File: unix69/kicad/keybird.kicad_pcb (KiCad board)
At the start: 2 copper layers, 142 parts, among them SW00 SW_Push, SW01 SW_Push, SW02 SW_Push, SW03 SW_Push, SW04 SW_Push, SW05 SW_Push, SW06 SW_Push, SW07 SW_Push, SW10 SW_Push, SW11 SW_Push, SW12 SW_Push, SW13 SW_Push, SW14 SW_Push, SW15 SW_Push, SW16 SW_Push, SW17 SW_Push, SW20 SW_Push, SW21 SW_Push, SW22 SW_Push, SW23 SW_Push, SW24 SW_Push, SW25 SW_Push, SW26 SW_Push, SW27 SW_Push, SW30 SW_Push, SW31 SW_Push, SW32 SW_Push, SW33 SW_Push, SW34 SW_Push, SW35 SW_Push, SW36 SW_Push, SW40 SW_Push, SW41 SW_Push, SW42 SW_Push, SW43 SW_Push, SW44 SW_Push, SW45 SW_Push, SW47 SW_Push, SW50 SW_Push, SW51 SW_Push, SW52 SW_Push, SW53 SW_Push, SW54 SW_Push, SW55 SW_Push, SW56 SW_Push, SW57 SW_Push, SW60 SW_Push, SW61 SW_Push, SW62 SW_Push, SW63 SW_Push, SW64 SW_Push, SW65 SW_Push, SW66 SW_Push, SW67 SW_Push, SW70 SW_Push, SW71 SW_Push, SW72 SW_Push, SW73 SW_Push, SW74 SW_Push, SW75 SW_Push, SW76 SW_Push, SW77 SW_Push, SW80 SW_Push, SW81 SW_Push, SW83 SW_Push, SW84 SW_Push, SW85 SW_Push, SW86 SW_Push, SW87 SW_Push, U0 RP2040-Tiny

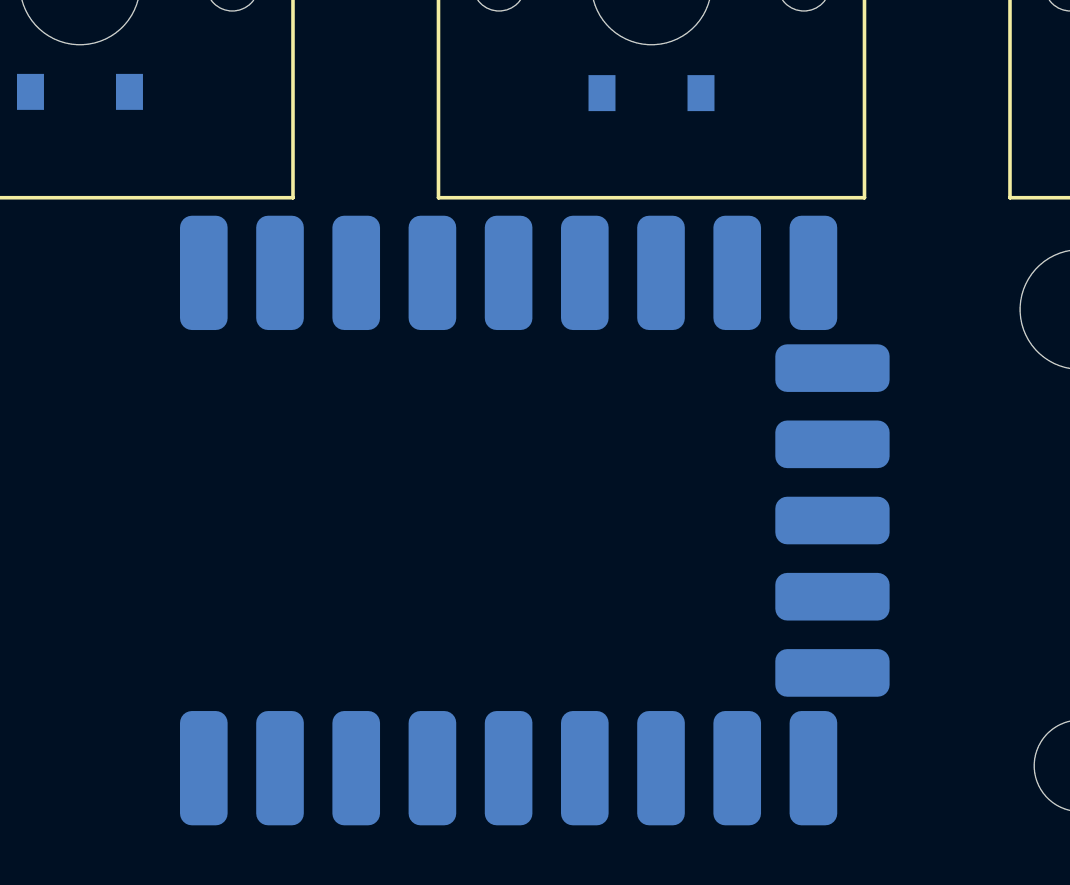
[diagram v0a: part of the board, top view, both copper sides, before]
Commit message: much pcb fettling
silkscreen key names from schematic

diode placement wrt switch connections
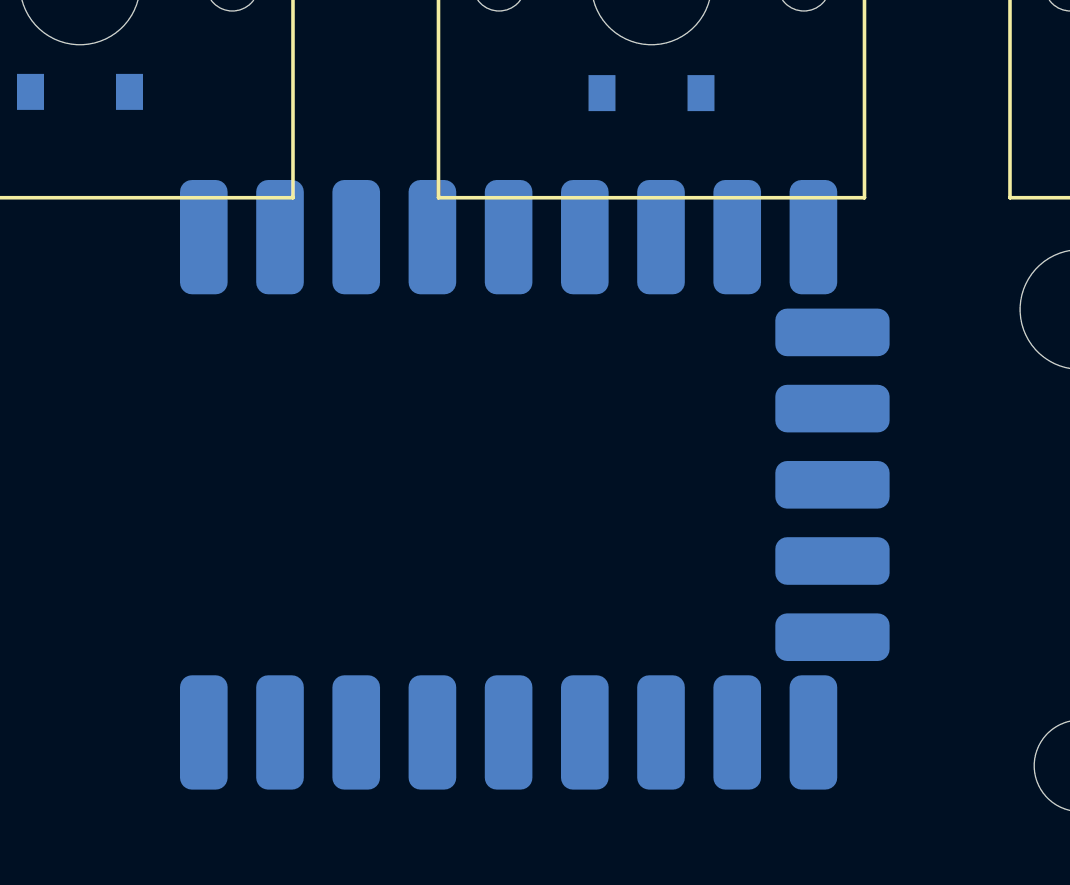
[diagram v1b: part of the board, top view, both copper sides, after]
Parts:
- SW00: value SW_Push -> ESC
- SW01: value SW_Push -> 2
- SW02: value SW_Push -> 4
- SW03: value SW_Push -> 6
- SW04: value SW_Push -> 8
- SW05: value SW_Push -> 0
- SW06: value SW_Push -> EQUAL
- SW07: value SW_Push -> GRAVE
- SW10: value SW_Push -> 1
- SW11: value SW_Push -> 3
- SW12: value SW_Push -> 5
- SW13: value SW_Push -> 7
- SW14: value SW_Push -> 9
- SW15: value SW_Push -> MINUS
- SW16: value SW_Push -> BSLS
- SW17: value SW_Push -> F16
- SW20: value SW_Push -> TAB
- SW21: value SW_Push -> W
- SW22: value SW_Push -> R
- SW23: value SW_Push -> Y
- SW24: value SW_Push -> I
- SW25: value SW_Push -> P
- SW26: value SW_Push -> RBRC
- SW27: value SW_Push -> F17
- SW30: value SW_Push -> Q
- SW31: value SW_Push -> E
- SW32: value SW_Push -> T
- SW33: value SW_Push -> U
- SW34: value SW_Push -> O
- SW35: value SW_Push -> LBRC
- SW36: value SW_Push -> BSPC
- SW40: value SW_Push -> A
- SW41: value SW_Push -> D
- SW42: value SW_Push -> G
- SW43: value SW_Push -> J
- SW44: value SW_Push -> L
- SW45: value SW_Push -> QUOTE
- SW47: value SW_Push -> F18
- SW50: value SW_Push -> LCTL
- SW51: value SW_Push -> S
- SW52: value SW_Push -> F
- SW53: value SW_Push -> H
- SW54: value SW_Push -> K
- SW55: value SW_Push -> SCLN
- SW56: value SW_Push -> ENTER
- SW57: value SW_Push -> F19
- SW60: value SW_Push -> LSFT
- SW61: value SW_Push -> X
- SW62: value SW_Push -> V
- SW63: value SW_Push -> N
- SW64: value SW_Push -> COMMA
- SW65: value SW_Push -> SLASH
- SW66: value SW_Push -> RSFT
- SW67: value SW_Push -> UP
- SW70: value SW_Push -> LFN
- SW71: value SW_Push -> Z
- SW72: value SW_Push -> C
- SW73: value SW_Push -> B
- SW74: value SW_Push -> M
- SW75: value SW_Push -> DOT
- SW76: value SW_Push -> LEFT
- SW77: value SW_Push -> RIGHT
- SW80: value SW_Push -> LALT
- SW81: value SW_Push -> LGUI
- SW83: value SW_Push -> SPACE
- SW84: value SW_Push -> RGUI
- SW85: value SW_Push -> RCTL
- SW86: value SW_Push -> RFN
- SW87: value SW_Push -> DOWN
- moved U0 1.19 mm to (176.2, 97.6)

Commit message: pcb edge and cutout for reset buttons
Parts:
- moved D04 8.06 mm to (179.8, 20.2), turned to 180 degrees
- moved D13 8.06 mm to (153.6, 20.2), turned to 180 degrees
- turned SW04 to 180 degrees
- turned SW13 to 180 degrees
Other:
- board outline added: 304.8 x 95.2 mm

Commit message: connecting tracks to diodes
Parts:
- moved D04 1.33 mm to (178.5, 20.2)
- moved D13 1.19 mm to (154.8, 20.2)
- moved D40 0.30 mm to (57.1, 65.5)
- moved D47 0.25 mm to (309.6, 65.5)
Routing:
- net /GP7: track 0.00 -> 10.7 mm
- net Net-(D04-Pad1): track 0.00 -> 10.7 mm
- net Net-(D17-Pad1): track 0.00 -> 9.90 mm
- net Net-(D64-Pad1): track 0.00 -> 9.68 mm
- net Net-(D87-Pad1): track 0.00 -> 9.68 mm
- net Net-(D67-Pad1): track 0.00 -> 9.68 mm
- net Net-(D75-Pad1): track 0.00 -> 9.68 mm
- net Net-(D65-Pad1): track 0.00 -> 9.68 mm
- net Net-(D07-Pad1): track 0.00 -> 9.68 mm
- net Net-(D86-Pad1): track 0.00 -> 9.68 mm
- net Net-(D06-Pad1): track 0.00 -> 9.68 mm
- net Net-(D74-Pad1): track 0.00 -> 9.68 mm
- net Net-(D73-Pad1): track 0.00 -> 9.68 mm
- net Net-(D63-Pad1): track 0.00 -> 9.68 mm
- net Net-(D62-Pad1): track 0.00 -> 9.68 mm
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
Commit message: redo the row lines on the front of the board
much nicer!
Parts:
- moved U2040 61.9 mm to (114.3, 98.2)
- moved D04 1.44 mm to (179.8, 19.6), turned to 0 degrees
- moved D13 1.14 mm to (153.8, 19.6), turned to 0 degrees
- moved D16 0.60 mm to (271.4, 28.0)
- moved D17 0.60 mm to (309.6, 28.0)
- moved D07 0.60 mm to (290.5, 28.0)
- moved D15 0.60 mm to (233.4, 28.0)
- moved D63 0.60 mm to (161.9, 85.1)
- moved D66 0.60 mm to (264.3, 85.1)
- moved D47 0.60 mm to (309.6, 66.1)
- moved D40 0.57 mm to (57.1, 66.1)
- moved D06 0.56 mm to (252.4, 28.0)
- moved D70 0.55 mm to (26.2, 104.2)
- moved D76 0.55 mm to (271.5, 104.2)
- moved D80 0.55 mm to (50.0, 104.2)
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- renumbered U0 to U2040
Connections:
- net /GP10 renamed /COL5
- net /GP11 renamed /COL6
- net /GP12 renamed /COL7
- net /GP13 renamed /COL3
- net /GP14 renamed /COL2
- net /GP15 renamed /COL1
- net /GP26 renamed /COL0
- net /GP4 renamed /ROW4
- net /GP9 renamed /COL4
- D00 pad 2: /GP8 -> /ROW0
- D01 pad 2: /GP8 -> /ROW0
- D02 pad 2: /GP8 -> /ROW0
- D03 pad 2: /GP8 -> /ROW0
- D04 pad 2: /GP8 -> /ROW0
- D05 pad 2: /GP8 -> /ROW0
- D06 pad 2: /GP8 -> /ROW0
- D07 pad 2: /GP8 -> /ROW0
- D10 pad 2: /GP7 -> /ROW1
- D11 pad 2: /GP7 -> /ROW1
- D12 pad 2: /GP7 -> /ROW1
- D13 pad 2: /GP7 -> /ROW1
- D14 pad 2: /GP7 -> /ROW1
- D15 pad 2: /GP7 -> /ROW1
- D16 pad 2: /GP7 -> /ROW1
- D17 pad 2: /GP7 -> /ROW1
- D20 pad 2: /GP6 -> /ROW2
- D21 pad 2: /GP6 -> /ROW2
- D22 pad 2: /GP6 -> /ROW2
- D23 pad 2: /GP6 -> /ROW2
- D24 pad 2: /GP6 -> /ROW2
- D25 pad 2: /GP6 -> /ROW2
- D26 pad 2: /GP6 -> /ROW2
- D27 pad 2: /GP6 -> /ROW2
- D30 pad 2: /GP5 -> /ROW3
- D31 pad 2: /GP5 -> /ROW3
- D32 pad 2: /GP5 -> /ROW3
- D33 pad 2: /GP5 -> /ROW3
- D34 pad 2: /GP5 -> /ROW3
- D35 pad 2: /GP5 -> /ROW3
- D36 pad 2: /GP5 -> /ROW3
- D50 pad 2: /GP3 -> /ROW5
- D51 pad 2: /GP3 -> /ROW5
- D52 pad 2: /GP3 -> /ROW5
- D53 pad 2: /GP3 -> /ROW5
- D54 pad 2: /GP3 -> /ROW5
- D55 pad 2: /GP3 -> /ROW5
- D56 pad 2: /GP3 -> /ROW5
- D57 pad 2: /GP3 -> /ROW5
- D60 pad 2: /GP2 -> /ROW6
- D61 pad 2: /GP2 -> /ROW6
- D62 pad 2: /GP2 -> /ROW6
- D63 pad 2: /GP2 -> /ROW6
- D64 pad 2: /GP2 -> /ROW6
- D65 pad 2: /GP2 -> /ROW6
- D66 pad 2: /GP2 -> /ROW6
- D67 pad 2: /GP2 -> /ROW6
- D70 pad 2: /GP1 -> /ROW7
- D71 pad 2: /GP1 -> /ROW7
- D72 pad 2: /GP1 -> /ROW7
- D73 pad 2: /GP1 -> /ROW7
- D74 pad 2: /GP1 -> /ROW7
- D75 pad 2: /GP1 -> /ROW7
- D76 pad 2: /GP1 -> /ROW7
- D77 pad 2: /GP1 -> /ROW7
- D80 pad 2: /GP0 -> /ROW8
- D81 pad 2: /GP0 -> /ROW8
- D83 pad 2: /GP0 -> /ROW8
- D84 pad 2: /GP0 -> /ROW8
- D85 pad 2: /GP0 -> /ROW8
- D86 pad 2: /GP0 -> /ROW8
- D87 pad 2: /GP0 -> /ROW8
- U2040 pad 0: /GP0 -> /ROW0
- U2040 pad 1: /GP1 -> /ROW1
- U2040 pad 2: /GP2 -> /ROW2
- U2040 pad 3: /GP3 -> /ROW3
- U2040 pad 5: /GP5 -> /ROW5
- U2040 pad 6: /GP6 -> /ROW6
- U2040 pad 7: /GP7 -> /ROW7
- U2040 pad 8: /GP8 -> /ROW8
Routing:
- net /ROW1: track 0.00 -> 514.9 mm, vias 0 -> 9
- net /ROW7: track 0.00 -> 507.3 mm, vias 0 -> 9
- net /ROW0: track 0.00 -> 493.8 mm, vias 0 -> 9
- net /ROW5: track 0.00 -> 488.4 mm, vias 0 -> 9
- net /ROW2: track 0.00 -> 476.6 mm, vias 0 -> 9
- net /ROW3: track 0.00 -> 447.8 mm, vias 0 -> 8
- net /ROW4: track 7.14 -> 453.4 mm, vias 0 -> 8
- net /ROW6: track 0.00 -> 421.3 mm, vias 0 -> 9
- net /ROW8: track 0.00 -> 267.0 mm, vias 0 -> 8
- net (no net): track 0.00 -> 186.3 mm, vias 69 -> 0
- net /GP7: track 10.7 -> 0.00 mm
- net /GP6: track 9.53 -> 0.00 mm
- net /GP3: track 9.53 -> 0.00 mm
- net /GP1: track 9.53 -> 0.00 mm
- net /GP2: track 9.53 -> 0.00 mm
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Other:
- board text added: "RP2040 is under here"
- board text added: "Tony Finch <dot@dotat.at>"
- board text added: "desiged and assembled"
- board text added: "in Cambridge by"
- board text added: "my usb port is too big"

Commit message: done? no drc errors!
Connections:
- U2040 pad 10: /COL5 -> /COL6
- U2040 pad 11: /COL6 -> /COL5
- U2040 pad 12: /COL7 -> /COL4
- U2040 pad 14: /COL2 -> /COL0
- U2040 pad 16: /COL0 -> /COL2
- U2040 pad 9: /COL4 -> /COL7
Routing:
- net /COL7: track 0.00 -> 323.4 mm
- net /COL6: track 0.00 -> 321.3 mm
- net /COL5: track 0.00 -> 294.3 mm
- net /COL0: track 0.00 -> 286.6 mm
- net /COL4: track 0.00 -> 260.7 mm
- net /COL1: track 0.00 -> 245.8 mm
- net /COL2: track 0.00 -> 197.0 mm
- net /COL3: track 0.00 -> 174.8 mm
- net /ROW4: track 453.4 -> 455.1 mm
- net Net-(D14-Pad1): track 9.58 -> 10.2 mm
- net Net-(D80-Pad1): track 10.7 -> 10.1 mm

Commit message: final version with rows on front
gonna start again, this time better
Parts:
- renumbered U2040 to U1
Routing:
- net /COL1: track 245.8 -> 236.7 mm
- net /COL5: track 294.3 -> 287.5 mm
- net /COL4: track 260.7 -> 254.6 mm
- net /COL2: track 197.0 -> 191.8 mm
- net /COL0: track 286.6 -> 289.8 mm
- net /COL6: track 321.3 -> 318.5 mm
- net /COL3: track 174.8 -> 172.2 mm
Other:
- board text added: "(delete)"
- board text added: "(return)"
- board text added: "S P A C E"
- board text added: "rows on the other side"

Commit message: major revision
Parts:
- removed D75: DIODE, Diode_SMD:D_SOD-123
- removed SW75: DOT, Switch_Keyboard_Hotswap_Kailh:SW_Hotswap_Kailh_MX_1.00u
- added D82: DIODE, Diode_SMD:D_SOD-123, B.Cu at (83.9, 100.0)
- added SW82: LMETA, Switch_Keyboard_Hotswap_Kailh:SW_Hotswap_Kailh_MX_1.25u, F.Cu at (73.8, 100.1)
- SW07: value GRAVE -> BQUOT
- SW16: value BSLS -> BSLSH
- SW17: value F16 -> F13
- SW26: value RBRC -> RBRAC
- SW27: value F17 -> F14
- SW35: value LBRC -> LBRAC
- SW36: value BSPC -> DEL
- SW47: value F18 -> F15
- SW50: value LCTL -> LCTRL
- SW55: value SCLN -> COLON
- SW56: value ENTER -> RET
- SW57: value F19 -> F16
- SW60: value LSFT -> LSHFT
- SW66: value RSFT -> RSHFT
- SW70: value LFN -> Z; footprint Switch_Keyboard_Hotswap_Kailh:SW_Hotswap_Kailh_MX_1.25u -> Switch_Keyboard_Hotswap_Kailh:SW_Hotswap_Kailh_MX_1.00u
- SW71: value Z -> C
- SW72: value C -> B
- SW73: value B -> M
- SW74: value M -> DOT
- SW80: value LALT -> LFUN
- SW81: value LGUI -> LALT
- SW84: value RGUI -> RMETA
- SW85: value RCTL -> RCTRL
- SW86: value RFN -> RFUN
- moved SW70 44.7 mm to (66.7, 81.0)
- moved D70 39.3 mm to (59.5, 83.3), turned to 90 degrees
- moved SW74 38.1 mm to (219.1, 81.0)
- moved SW73 38.1 mm to (181.0, 81.0)
- moved SW72 38.1 mm to (142.9, 81.0)
- moved SW71 38.1 mm to (104.8, 81.0)
- moved D74 31.0 mm to (211.9, 83.3), turned to 90 degrees
- moved D73 31.0 mm to (173.8, 83.3), turned to 90 degrees
- moved D72 31.0 mm to (135.7, 83.3), turned to 90 degrees
- moved D71 31.0 mm to (97.6, 83.3), turned to 90 degrees
- moved SW80 23.8 mm to (26.2, 100.0), turned to 180 degrees
- moved SW81 23.8 mm to (50.0, 100.0), turned to 180 degrees
- moved D13 15.9 mm to (165.0, 30.9), turned to 90 degrees
- moved D80 14.3 mm to (36.3, 100.0), turned to -90 degrees
- moved D81 14.3 mm to (60.1, 100.0), turned to -90 degrees
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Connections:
- D70 pad 1: Net-(D70-Pad1) -> Net-(SW70-Pad1)
- D71 pad 1: Net-(D71-Pad1) -> Net-(SW71-Pad1)
- D72 pad 1: Net-(D72-Pad1) -> Net-(SW72-Pad1)
- D73 pad 1: Net-(D73-Pad1) -> Net-(SW73-Pad1)
- D74 pad 1: Net-(D74-Pad1) -> Net-(SW74-Pad1)
- D76 pad 1: Net-(D76-Pad1) -> Net-(SW76-Pad1)
- SW00 pad 1: /COL0 -> Net-(D00-Pad1)
- SW00 pad 2: Net-(D00-Pad1) -> /COL0
- SW01 pad 1: /COL1 -> Net-(D01-Pad1)
- SW01 pad 2: Net-(D01-Pad1) -> /COL1
- SW02 pad 1: /COL2 -> Net-(D02-Pad1)
- SW02 pad 2: Net-(D02-Pad1) -> /COL2
- SW03 pad 1: /COL3 -> Net-(D03-Pad1)
- SW03 pad 2: Net-(D03-Pad1) -> /COL3
- SW04 pad 1: /COL4 -> Net-(D04-Pad1)
- SW04 pad 2: Net-(D04-Pad1) -> /COL4
- SW05 pad 1: /COL5 -> Net-(D05-Pad1)
- SW05 pad 2: Net-(D05-Pad1) -> /COL5
- SW06 pad 1: /COL6 -> Net-(D06-Pad1)
- SW06 pad 2: Net-(D06-Pad1) -> /COL6
- SW07 pad 1: /COL7 -> Net-(D07-Pad1)
- SW07 pad 2: Net-(D07-Pad1) -> /COL7
- SW10 pad 1: /COL0 -> Net-(D10-Pad1)
- SW10 pad 2: Net-(D10-Pad1) -> /COL0
- SW11 pad 1: /COL1 -> Net-(D11-Pad1)
- SW11 pad 2: Net-(D11-Pad1) -> /COL1
- SW12 pad 1: /COL2 -> Net-(D12-Pad1)
- SW12 pad 2: Net-(D12-Pad1) -> /COL2
- SW13 pad 1: /COL3 -> Net-(D13-Pad1)
- SW13 pad 2: Net-(D13-Pad1) -> /COL3
- SW14 pad 1: /COL4 -> Net-(D14-Pad1)
- SW14 pad 2: Net-(D14-Pad1) -> /COL4
- SW15 pad 1: /COL5 -> Net-(D15-Pad1)
- SW15 pad 2: Net-(D15-Pad1) -> /COL5
- SW16 pad 1: /COL6 -> Net-(D16-Pad1)
- SW16 pad 2: Net-(D16-Pad1) -> /COL6
- SW17 pad 1: /COL7 -> Net-(D17-Pad1)
- SW17 pad 2: Net-(D17-Pad1) -> /COL7
- SW20 pad 1: /COL0 -> Net-(D20-Pad1)
- SW20 pad 2: Net-(D20-Pad1) -> /COL0
- SW21 pad 1: /COL1 -> Net-(D21-Pad1)
- SW21 pad 2: Net-(D21-Pad1) -> /COL1
- SW22 pad 1: /COL2 -> Net-(D22-Pad1)
- SW22 pad 2: Net-(D22-Pad1) -> /COL2
- SW23 pad 1: /COL3 -> Net-(D23-Pad1)
- SW23 pad 2: Net-(D23-Pad1) -> /COL3
- SW24 pad 1: /COL4 -> Net-(D24-Pad1)
- SW24 pad 2: Net-(D24-Pad1) -> /COL4
- SW25 pad 1: /COL5 -> Net-(D25-Pad1)
- SW25 pad 2: Net-(D25-Pad1) -> /COL5
- SW26 pad 1: /COL6 -> Net-(D26-Pad1)
- SW26 pad 2: Net-(D26-Pad1) -> /COL6
- SW27 pad 1: /COL7 -> Net-(D27-Pad1)
- SW27 pad 2: Net-(D27-Pad1) -> /COL7
- SW30 pad 1: /COL0 -> Net-(D30-Pad1)
- SW30 pad 2: Net-(D30-Pad1) -> /COL0
- SW31 pad 1: /COL1 -> Net-(D31-Pad1)
- SW31 pad 2: Net-(D31-Pad1) -> /COL1
- SW32 pad 1: /COL2 -> Net-(D32-Pad1)
- SW32 pad 2: Net-(D32-Pad1) -> /COL2
- SW33 pad 1: /COL3 -> Net-(D33-Pad1)
- SW33 pad 2: Net-(D33-Pad1) -> /COL3
- SW34 pad 1: /COL4 -> Net-(D34-Pad1)
- SW34 pad 2: Net-(D34-Pad1) -> /COL4
- SW35 pad 1: /COL5 -> Net-(D35-Pad1)
- SW35 pad 2: Net-(D35-Pad1) -> /COL5
- SW36 pad 1: /COL6 -> Net-(D36-Pad1)
- SW36 pad 2: Net-(D36-Pad1) -> /COL6
- SW40 pad 1: /COL0 -> Net-(D40-Pad1)
- SW40 pad 2: Net-(D40-Pad1) -> /COL0
- SW41 pad 1: /COL1 -> Net-(D41-Pad1)
- SW41 pad 2: Net-(D41-Pad1) -> /COL1
- SW42 pad 1: /COL2 -> Net-(D42-Pad1)
- SW42 pad 2: Net-(D42-Pad1) -> /COL2
- SW43 pad 1: /COL3 -> Net-(D43-Pad1)
- SW43 pad 2: Net-(D43-Pad1) -> /COL3
- SW44 pad 1: /COL4 -> Net-(D44-Pad1)
- SW44 pad 2: Net-(D44-Pad1) -> /COL4
- SW45 pad 1: /COL5 -> Net-(D45-Pad1)
- SW45 pad 2: Net-(D45-Pad1) -> /COL5
- SW47 pad 1: /COL7 -> Net-(D47-Pad1)
- SW47 pad 2: Net-(D47-Pad1) -> /COL7
- SW50 pad 1: /COL0 -> Net-(D50-Pad1)
- SW50 pad 2: Net-(D50-Pad1) -> /COL0
- SW51 pad 1: /COL1 -> Net-(D51-Pad1)
- SW51 pad 2: Net-(D51-Pad1) -> /COL1
- SW52 pad 1: /COL2 -> Net-(D52-Pad1)
- SW52 pad 2: Net-(D52-Pad1) -> /COL2
- SW53 pad 1: /COL3 -> Net-(D53-Pad1)
- SW53 pad 2: Net-(D53-Pad1) -> /COL3
- SW54 pad 1: /COL4 -> Net-(D54-Pad1)
- SW54 pad 2: Net-(D54-Pad1) -> /COL4
- SW55 pad 1: /COL5 -> Net-(D55-Pad1)
- SW55 pad 2: Net-(D55-Pad1) -> /COL5
- SW56 pad 1: /COL6 -> Net-(D56-Pad1)
- SW56 pad 2: Net-(D56-Pad1) -> /COL6
- SW57 pad 1: /COL7 -> Net-(D57-Pad1)
- SW57 pad 2: Net-(D57-Pad1) -> /COL7
- SW60 pad 1: /COL0 -> Net-(D60-Pad1)
- SW60 pad 2: Net-(D60-Pad1) -> /COL0
- SW61 pad 1: /COL1 -> Net-(D61-Pad1)
- SW61 pad 2: Net-(D61-Pad1) -> /COL1
- SW62 pad 1: /COL2 -> Net-(D62-Pad1)
- SW62 pad 2: Net-(D62-Pad1) -> /COL2
- SW63 pad 1: /COL3 -> Net-(D63-Pad1)
- SW63 pad 2: Net-(D63-Pad1) -> /COL3
- SW64 pad 1: /COL4 -> Net-(D64-Pad1)
- SW64 pad 2: Net-(D64-Pad1) -> /COL4
- SW65 pad 1: /COL5 -> Net-(D65-Pad1)
- SW65 pad 2: Net-(D65-Pad1) -> /COL5
- SW66 pad 1: /COL6 -> Net-(D66-Pad1)
- SW66 pad 2: Net-(D66-Pad1) -> /COL6
- SW67 pad 1: /COL7 -> Net-(D67-Pad1)
- SW67 pad 2: Net-(D67-Pad1) -> /COL7
- SW70 pad 1: /COL0 -> Net-(SW70-Pad1)
- SW70 pad 2: Net-(D70-Pad1) -> /COL0
- SW71 pad 1: /COL1 -> Net-(SW71-Pad1)
- SW71 pad 2: Net-(D71-Pad1) -> /COL1
- SW72 pad 1: /COL2 -> Net-(SW72-Pad1)
- SW72 pad 2: Net-(D72-Pad1) -> /COL2
- SW73 pad 1: /COL3 -> Net-(SW73-Pad1)
- SW73 pad 2: Net-(D73-Pad1) -> /COL3
- SW74 pad 1: /COL4 -> Net-(SW74-Pad1)
- SW74 pad 2: Net-(D74-Pad1) -> /COL4
- SW76 pad 1: /COL6 -> Net-(SW76-Pad1)
- SW76 pad 2: Net-(D76-Pad1) -> /COL6
- SW77 pad 1: /COL7 -> Net-(D77-Pad1)
- SW77 pad 2: Net-(D77-Pad1) -> /COL7
- SW80 pad 1: /COL0 -> Net-(D80-Pad1)
- SW80 pad 2: Net-(D80-Pad1) -> /COL0
- SW81 pad 1: /COL1 -> Net-(D81-Pad1)
- SW81 pad 2: Net-(D81-Pad1) -> /COL1
- SW83 pad 1: /COL3 -> Net-(D83-Pad1)
- SW83 pad 2: Net-(D83-Pad1) -> /COL3
- SW84 pad 1: /COL4 -> Net-(D84-Pad1)
- SW84 pad 2: Net-(D84-Pad1) -> /COL4
- SW85 pad 1: /COL5 -> Net-(D85-Pad1)
- SW85 pad 2: Net-(D85-Pad1) -> /COL5
- SW86 pad 1: /COL6 -> Net-(D86-Pad1)
- SW86 pad 2: Net-(D86-Pad1) -> /COL6
- SW87 pad 1: /COL7 -> Net-(D87-Pad1)
- SW87 pad 2: Net-(D87-Pad1) -> /COL7
- U1 pad 0: /ROW0 -> /COL0
- U1 pad 1: /ROW1 -> /COL1
- U1 pad 10: /COL6 -> /ROW1
- U1 pad 11: /COL5 -> /ROW2
- U1 pad 12: /COL4 -> /ROW3
- U1 pad 13: /COL3 -> /ROW4
- U1 pad 14: /COL0 -> /ROW5
- U1 pad 15: /COL1 -> /ROW6
- U1 pad 16: /COL2 -> /ROW7
- U1 pad 2: /ROW2 -> /COL2
- U1 pad 3: /ROW3 -> /COL3
- U1 pad 4: /ROW4 -> /COL7
- U1 pad 5: /ROW5 -> /COL6
- U1 pad 6: /ROW6 -> /COL5
- U1 pad 7: /ROW7 -> /COL4
- U1 pad 9: /COL7 -> /ROW0
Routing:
- net (no net): track 186.3 -> 0.00 mm
- net /ROW7: track 507.1 -> 413.2 mm, vias 9 -> 0
- net /COL2: track 191.8 -> 259.9 mm, vias 0 -> 10
- net /COL4: track 254.6 -> 316.3 mm, vias 0 -> 10
- net /COL1: track 236.7 -> 290.9 mm, vias 0 -> 10
- net /COL3: track 172.2 -> 223.8 mm, vias 0 -> 10
- net /ROW6: track 421.0 -> 371.6 mm, vias 9 -> 0
- net /ROW1: track 514.4 -> 468.6 mm, vias 9 -> 0
- net /ROW0: track 493.6 -> 452.4 mm, vias 9 -> 0
- net /COL7: track 323.0 -> 358.1 mm, vias 0 -> 9
- net /COL6: track 318.5 -> 351.1 mm, vias 0 -> 9
- net /ROW4: track 454.9 -> 430.7 mm, vias 8 -> 0
- net /ROW2: track 476.4 -> 453.0 mm, vias 9 -> 0
- net /ROW3: track 447.6 -> 425.6 mm, vias 8 -> 0
- net /COL5: track 287.5 -> 307.2 mm, vias 0 -> 9
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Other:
- board text added: "USB"
- board text added: "keybird rev 0.2"
- board text removed: "(delete)"
- board text removed: "(return)"
- board text removed: "rows on the other side"

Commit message: very nice, i think
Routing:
- net /COL4: track 316.3 -> 307.2 mm
- net /COL7: track 358.1 -> 364.7 mm
- net /COL6: track 351.1 -> 346.2 mm
- net /COL2: track 259.9 -> 255.1 mm
- net /COL1: track 290.9 -> 288.6 mm
- net /COL0: track 297.0 -> 299.1 mm
- net /COL5: track 307.2 -> 308.5 mm
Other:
- board text added: "keybird"
- board text added: "rev 0.2"
- board text added: "to or for by with or from everybody"
- board text removed: "keybird rev 0.2"
